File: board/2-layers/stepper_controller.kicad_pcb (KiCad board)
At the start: 2 copper layers, 99 x 37 mm, 94 parts, among them J201 USB_OTG, P101 JTAG, P102 M3_AOUT, P103 M3_BOUT, P104 M2_AOUT, P105 M2_BOUT, P106 M1_AOUT, P107 M1_BOUT, P201 UART1, P203 PWM_OUT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

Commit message: done spartan 3a schematic
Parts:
- added U1: XC3S200A, TQFP_100, F.Cu at (167.9, 76.2)
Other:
- board outline removed

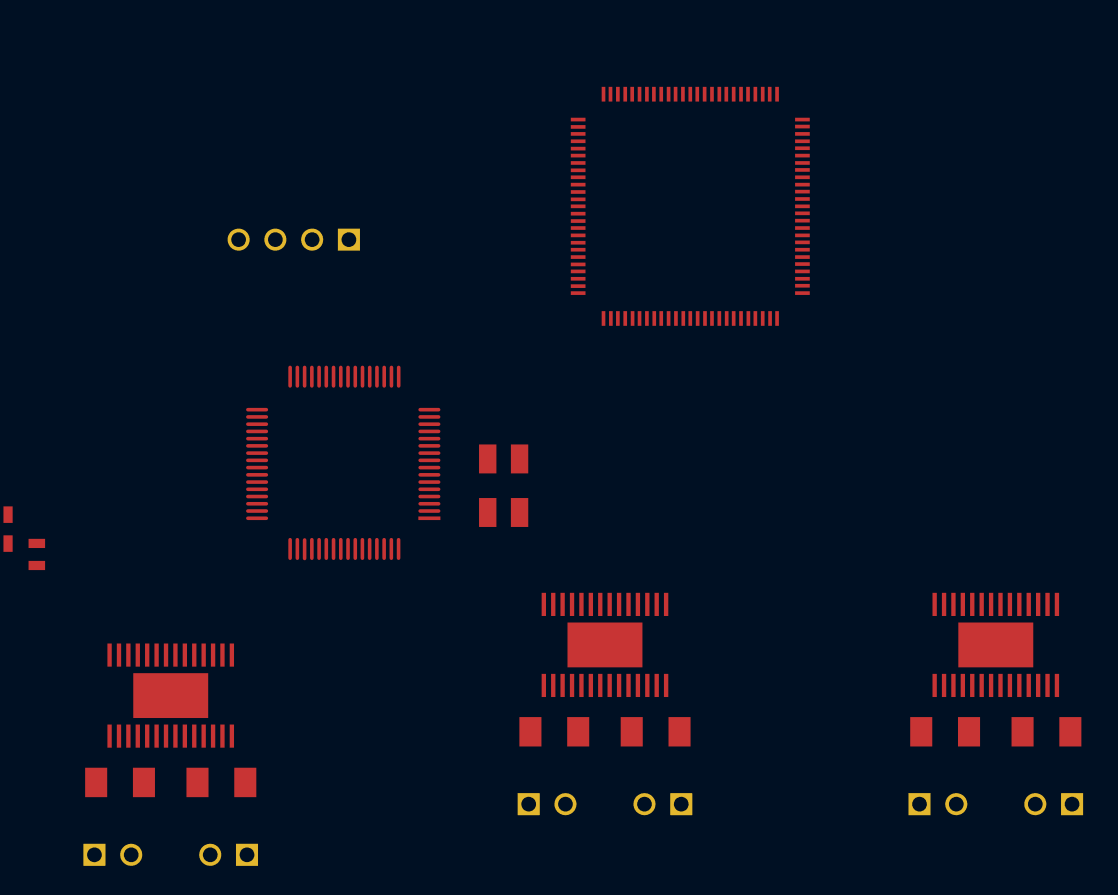
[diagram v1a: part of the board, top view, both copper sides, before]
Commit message: added fpga configuration
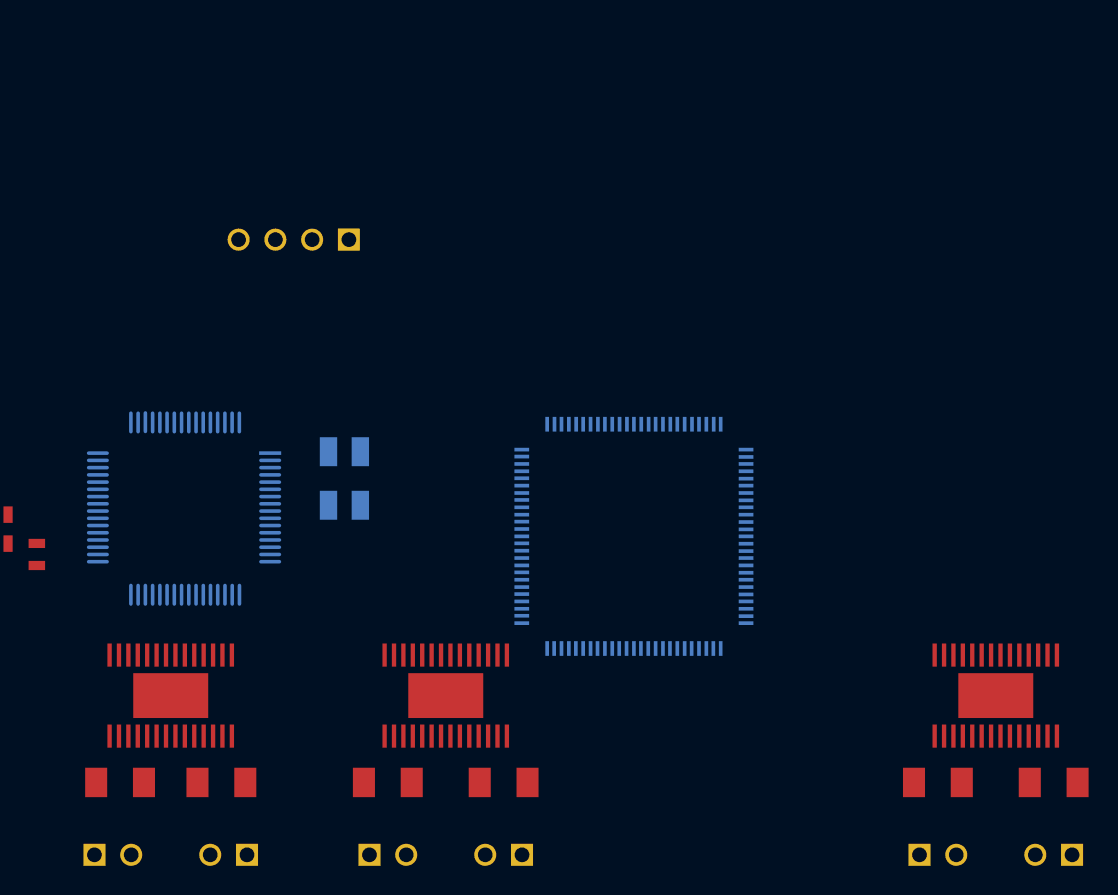
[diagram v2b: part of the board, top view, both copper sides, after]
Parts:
- U1, U202, X201: moved to B.Cu
- moved U1 23.1 mm to (164.0, 99.0)
- moved R118 12.0 mm to (147.0, 116.0)
- moved P106 11.5 mm to (147.0, 121.0)
- moved P107 11.5 mm to (155.0, 121.0)
- moved U104 11.5 mm to (151.0, 110.0)
- moved U202 11.4 mm to (133.0, 97.0), turned to 270 degrees
- moved R115 11.1 mm to (155.0, 116.0)
- moved X201 11.0 mm to (144.0, 95.0), turned to 270 degrees
- moved R114 3.54 mm to (193.0, 116.0)
- moved R117 3.54 mm to (185.0, 116.0)
- moved P104 3.50 mm to (185.0, 121.0)
- moved P105 3.50 mm to (193.0, 121.0)
- moved U103 3.50 mm to (189.0, 110.0)

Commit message: added 1.2V schematic
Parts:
- removed C101, C102, C103: 0.47u, SM0603
- removed C104, C105, C106: 0.1u, SM0603
- removed C107, C108, C109: 10n, SM0603
- removed C110, C111: 4.7u, SM0603
- removed C112, C113, C114, C118: 4.7u, SM0805
- removed C115, C116, C117: 4.7u, SM0603_Capa
- removed C201, C203, C204, C205, C206, C207, C209: 1uF, SM0603_Capa
- removed C202, C208: CSMALL, SM0603_Capa
- removed C301: 10uF 35V, SM1206
- removed C302: 10uF/35V, SM1206
- removed C303: 4.7nF, SM0603_Capa
- removed C304: 0.1uF, SM0805
- removed C305: 10nF, SM0805
- removed C306: 47uF, SM1210
- removed C307, C308: 1uF, SM0805
- removed C309: 4.7uF, SM0805
- removed D201: FAULT_RED, LED-0603
- removed D202: BUSY_ORANGE, LED-0603
- removed D203: POWER_GREEN, LED-0603
- removed D301: BAS16, SOD923
- removed J201: USB_OTG, Molex_54819-0572
- removed L301: 10uH, IND_7x7x4.5
- removed P101: JTAG, PIN_ARRAY-6X1
- removed P102: M3_AOUT, PIN_ARRAY_2X1
- removed P103: M3_BOUT, PIN_ARRAY_2X1
- removed P104: M2_AOUT, PIN_ARRAY_2X1
- removed P105: M2_BOUT, PIN_ARRAY_2X1
- removed P106: M1_AOUT, PIN_ARRAY_2X1
- removed P107: M1_BOUT, PIN_ARRAY_2X1
- removed P201: UART1, PIN_ARRAY_4x1
- removed P203: PWM_OUT, PIN_ARRAY_4x1
- removed P205: IR_FORK_CONN, pin_array_6
- removed P301: 12V_Conn, MOL_CONN_2_VH
- removed R101, R102, R103, R104, R105, R106, R202, R203: 0, SM0603
- removed R107, R109, R111: 4.7k, SM0603
- removed R108, R110, R112: 1k, SM0603
- removed R113, R114, R115, R116, R117, R118: 0.1, SM1206
- removed R201, R204, R304: 10k, SM0603
- removed R205, R206: 22, SM0603
- removed R207: 1.5k, SM0603
- removed R210, R211, R212: ?, SM0603
- removed R213, R214: 100, SM0603
- removed R301: 100k, SM0603
- removed R302: 4.42k, SM0603
- removed R303: 47k, SM0603
- removed R305: 30.9k, SM0603
- removed U1: XC3S200A, TQFP_100
- removed U102, U103, U104: DRV8825, HTSSOP28_PowerPad
- removed U202: STM32F103RG_LQFP64, TQFP_64
- removed U301: MP2303_SOIC8E, SOIC8_EPad
- removed X201: TXC_50X32_AB, XTAL_5.0x3.2mm
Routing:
- net (no net): track 617.2 -> 0.00 mm, vias 68 -> 0
- net +3.3V: track 148.0 -> 0.00 mm, vias 14 -> 0
- net +12V: track 80.9 -> 0.00 mm, vias 10 -> 0
- net N-0000063: track 24.0 -> 0.00 mm, vias 1 -> 0
- net N-0000064: track 23.7 -> 0.00 mm, vias 1 -> 0
- net N-0000083: track 22.8 -> 0.00 mm, vias 1 -> 0
- net EXT_JTAG_TMS: track 22.6 -> 0.00 mm, vias 1 -> 0
- net GND: track 21.8 -> 0.00 mm, vias 12 -> 0
- net N-0000087: track 17.9 -> 0.00 mm
- net N-0000071: track 16.6 -> 0.00 mm, vias 1 -> 0
- net EXT_JTAG_TCK: track 16.6 -> 0.00 mm, vias 1 -> 0
- net N-0000070: track 16.0 -> 0.00 mm, vias 1 -> 0
- net EXT_JTAG_TDO: track 15.2 -> 0.00 mm, vias 1 -> 0
- net EXT_JTAG_TDI: track 15.2 -> 0.00 mm, vias 1 -> 0
- net N-0000068: track 11.3 -> 0.00 mm
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- removed copper zone on F.Cu, net +3.3V
- removed copper zone on F.Cu, net /PSU/DC_SW
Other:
- board text removed: "+3.3"
- board text removed: "H"
- board text removed: "L"
- board text removed: "TCK"
- board text removed: "TDI"
- board text removed: "TDO"
- board text removed: "TMS"

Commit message: prout
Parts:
- added U101: DRV8825, HTSSOP28_PowerPad, F.Cu at (192.2, 114.8)
- added U102: DRV8825, HTSSOP28_PowerPad, F.Cu at (162.2, 114.8)
- added U103: DRV8825, HTSSOP28_PowerPad, F.Cu at (132.2, 114.5)
- added U201: STM32F103RG_LQFP64, LQFP_64, F.Cu at (133.0, 97.5)
- added U401: XC3S200A, TQFP_100, F.Cu at (159.8, 97.5)
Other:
- board outline added: 99 x 37 mm

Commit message: added dac start routing
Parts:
- added U104: MAX5713/4/5-TSSOP14, SSOP14, B.Cu at (160.0, 99.1)
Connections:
- U101 pad 16: nRESET -> /FPGA/M2_RESET
- U101 pad 17: nRESET -> /FPGA/M2_RESET
- U101 pad 20: (no net) -> /FPGA/M2_DIR
- U101 pad 21: (no net) -> /FPGA/M2_EN
- U101 pad 22: STEP -> /FPGA/M2_STEP
- U101 pad 24: MODE0 -> /FPGA/M2_MODE0
- U101 pad 25: MODE1 -> /FPGA/M2_MODE1
- U101 pad 26: MODE2 -> /FPGA/M2_MODE2
- U102 pad 16: nRESET -> /FPGA/M1_RESET
- U102 pad 17: nRESET -> /FPGA/M1_RESET
- U102 pad 20: (no net) -> /FPGA/M1_DIR
- U102 pad 21: (no net) -> /FPGA/M1_EN
- U102 pad 22: STEP -> /FPGA/M1_STEP
- U102 pad 24: MODE0 -> /FPGA/M1_MODE0
- U102 pad 25: MODE1 -> /FPGA/M1_MODE1
- U102 pad 26: MODE2 -> /FPGA/M1_MODE2
- U201 pad 2: (no net) -> /STM32//CLR_DAC
- U401 pad 10: (no net) -> /FPGA/M2_DIR
- U401 pad 11: (no net) -> +3.3V
- U401 pad 13: (no net) -> /FPGA/M2_RESET
- U401 pad 3: (no net) -> /FPGA/M2_MODE2
- U401 pad 4: (no net) -> /FPGA/M2_MODE1
- U401 pad 5: (no net) -> /FPGA/M2_MODE0
- U401 pad 6: (no net) -> /FPGA/M2_STEP
- U401 pad 77: (no net) -> /FPGA/M1_MODE2
- U401 pad 78: (no net) -> /FPGA/M1_MODE1
- U401 pad 83: (no net) -> /FPGA/M1_MODE0
- U401 pad 84: (no net) -> /FPGA/M1_STEP
- U401 pad 86: (no net) -> /FPGA/M1_EN
- U401 pad 88: (no net) -> /FPGA/M1_DIR
- U401 pad 9: (no net) -> /FPGA/M2_EN
- U401 pad 93: (no net) -> /FPGA/M1_RESET
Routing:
- net /VRF_2: track 0.00 -> 54.8 mm, vias 0 -> 1
- net /FPGA/M2_RESET: track 0.00 -> 36.8 mm
- net /FPGA/M2_DIR: track 0.00 -> 33.2 mm
- net /FPGA/M2_EN: track 0.00 -> 31.6 mm
- net /FPGA/M2_STEP: track 0.00 -> 30.1 mm
- net /FPGA/M2_MODE0: track 0.00 -> 28.9 mm
- net /FPGA/M2_MODE1: track 0.00 -> 27.8 mm
- net /FPGA/M2_MODE2: track 0.00 -> 26.9 mm
- net /VRF_1: track 0.00 -> 24.4 mm, vias 0 -> 1
- net /FPGA/DONE: track 0.00 -> 13.6 mm
- net /FPGA/COM_CS: track 0.00 -> 13.3 mm, vias 0 -> 1
- net /FPGA/COM_CLK: track 0.00 -> 10.8 mm, vias 0 -> 1
- net /FPGA/M1_MODE1: track 0.00 -> 9.69 mm
- net /FPGA/M1_MODE2: track 0.00 -> 9.56 mm
- net /FPGA/COM_MOSI: track 0.00 -> 8.74 mm, vias 0 -> 1
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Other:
- board outline removed

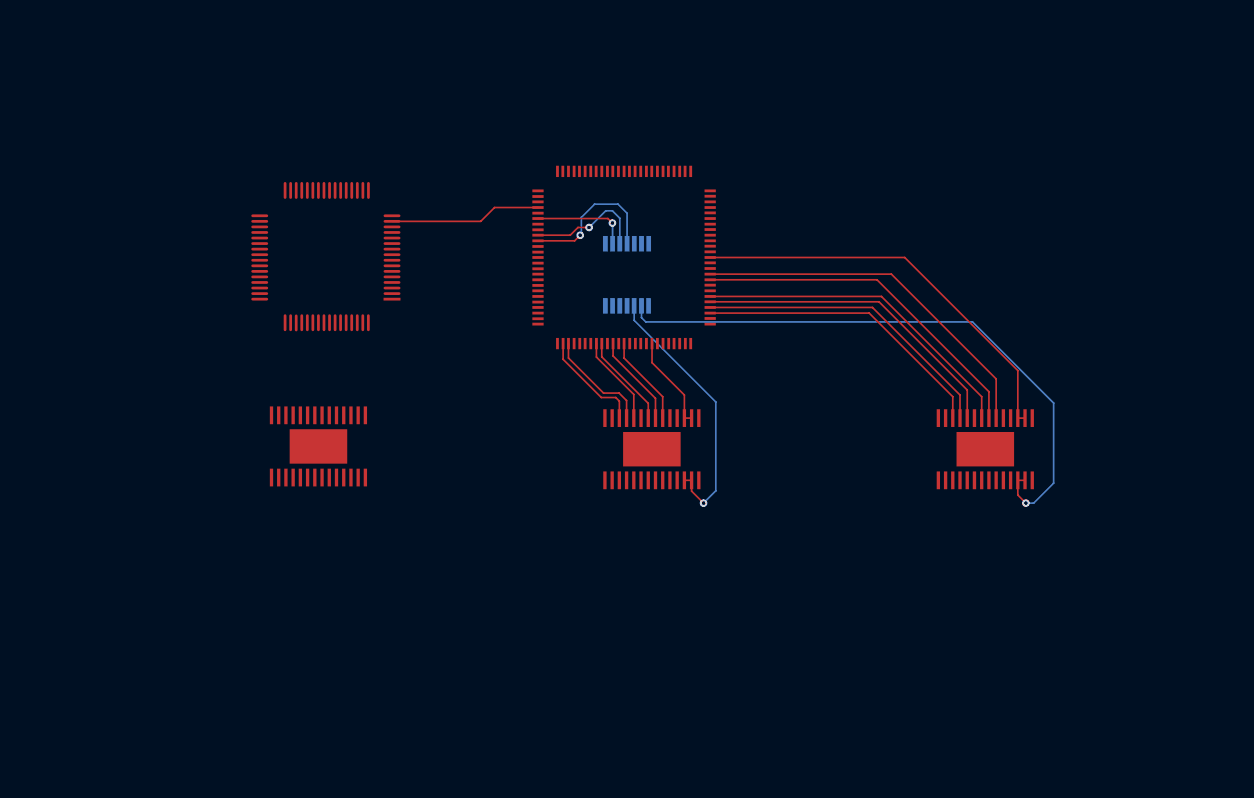
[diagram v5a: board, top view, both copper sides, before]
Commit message: placing USB and motor connector
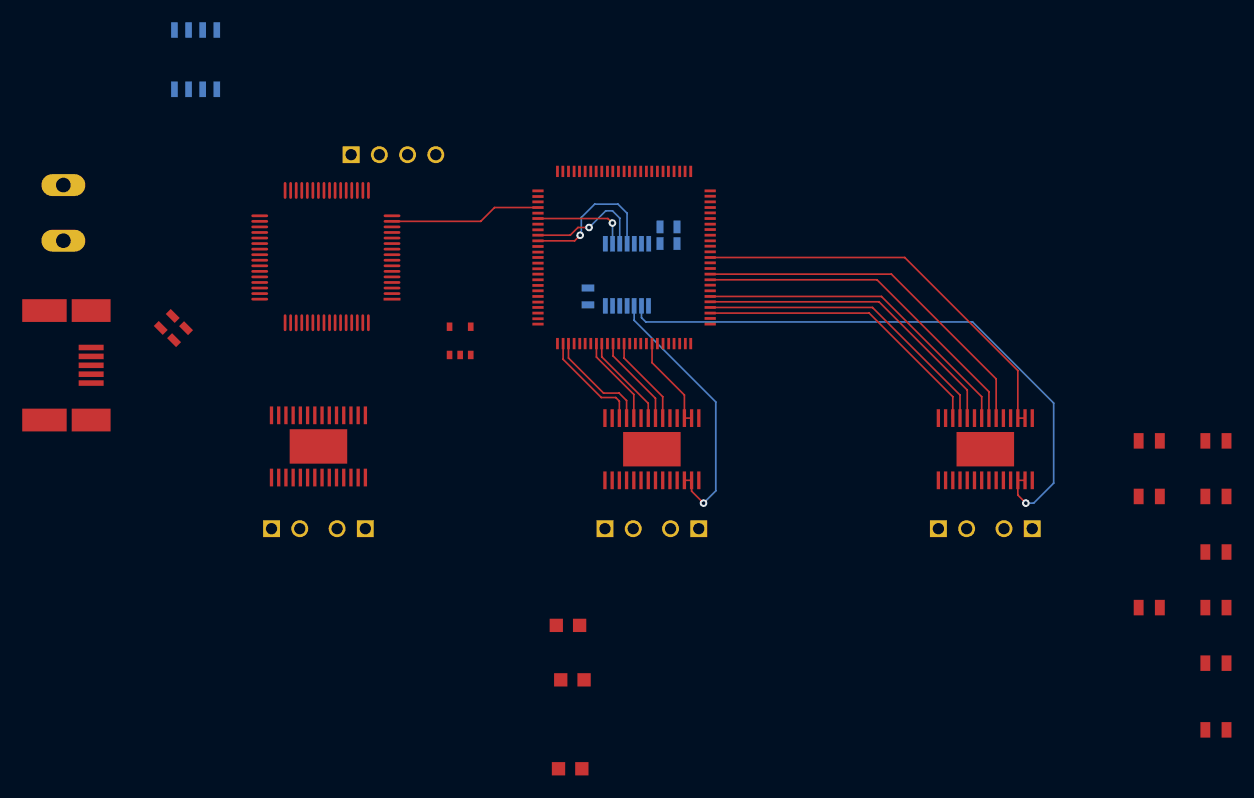
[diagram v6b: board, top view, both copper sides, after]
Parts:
- added C110: 4.7u, SM0805, F.Cu at (207.0, 129.0)
- added C111: 4.7u, SM0805, F.Cu at (213.0, 124.0)
- added C112: 4.7u, SM0805, F.Cu at (207.0, 114.0)
- added C113: 4.7u, SM0805, F.Cu at (207.0, 119.0)
- added C114: 4.7u, SM0805, F.Cu at (213.0, 129.0)
- added C115: 4.7u, SM0805, F.Cu at (213.0, 140.0)
- added C116: 4.7u, SM0805, F.Cu at (213.0, 119.0)
- added C117: 4.7u, SM0805, F.Cu at (213.0, 134.0)
- added C118: 4.7u, SM0805, F.Cu at (213.0, 114.0)
- added C119: 1u, SM0603_Capa, B.Cu at (156.5, 101.0)
- added C120: 0.1u, SM0603_Capa, B.Cu at (163.8, 94.8)
- added C121: 10n, SM0603_Capa, B.Cu at (163.8, 96.2)
- added D201: FAULT_RED, LED-0805, F.Cu at (154.7, 130.6)
- added D202: BUSY_ORANGE, LED-0805, F.Cu at (155.1, 135.5)
- added D203: POWER_GREEN, LED-0805, F.Cu at (154.9, 143.5)
- added J201: USB_OTG, Molex_54819-0572, F.Cu at (107.8, 107.2)
- added P103: M3_AOUT, PIN_ARRAY_2X1, F.Cu at (189.3, 121.9)
- added P104: M3_BOUT, PIN_ARRAY_2X1, F.Cu at (195.2, 121.9)
- added P105: M2_AOUT, PIN_ARRAY_2X1, F.Cu at (159.3, 121.9)
- added P106: M2_BOUT, PIN_ARRAY_2X1, F.Cu at (165.2, 121.9)
- added P107: M1_AOUT, PIN_ARRAY_2X1, F.Cu at (129.3, 121.9)
- added P108: M1_BOUT, PIN_ARRAY_2X1, F.Cu at (135.2, 121.9)
- added P201: UART1, PIN_ARRAY_4x1, F.Cu at (139.0, 88.2)
- added P301: 12V_Conn, MOL_CONN_2_VH, F.Cu at (109.3, 93.5)
- added R207: 22, SM0603, F.Cu at (119.8, 104.4)
- added R208: 22, SM0603, F.Cu at (118.6, 103.3)
- added U301: MP2128-SOT23, SOT23-5, F.Cu at (145.0, 105.0)
- added U302: MP2303_SOIC8E, SO8E, B.Cu at (121.2, 79.7)
